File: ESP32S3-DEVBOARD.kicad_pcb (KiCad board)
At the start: 2 copper layers, 33 x 58.4 mm, 61 parts, among them J1 PinHeader_1x22_P2.54mm_Vertic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, J2 PinHeader_1x22_P2.54mm_Vertic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, J3 G-Switch_GT-USB-7010ASV, J4 G-Switch_GT-USB-7010ASV, Q1 BC817-40,215, Q2 BC817-40,215, SW1 TS-1088-AR02016, SW2 TS-1088-AR02016, SW3 TS-1088-AR02016, SW4 TS-1088-AR02016, U1 AMS1117-3.3, U2 ESP32-S3-WROOM-1, U3 USBLC6-2P6, U4 CP2102N-A02-GQFN28R, U5 BMI270, U6 USBLC6-2P6

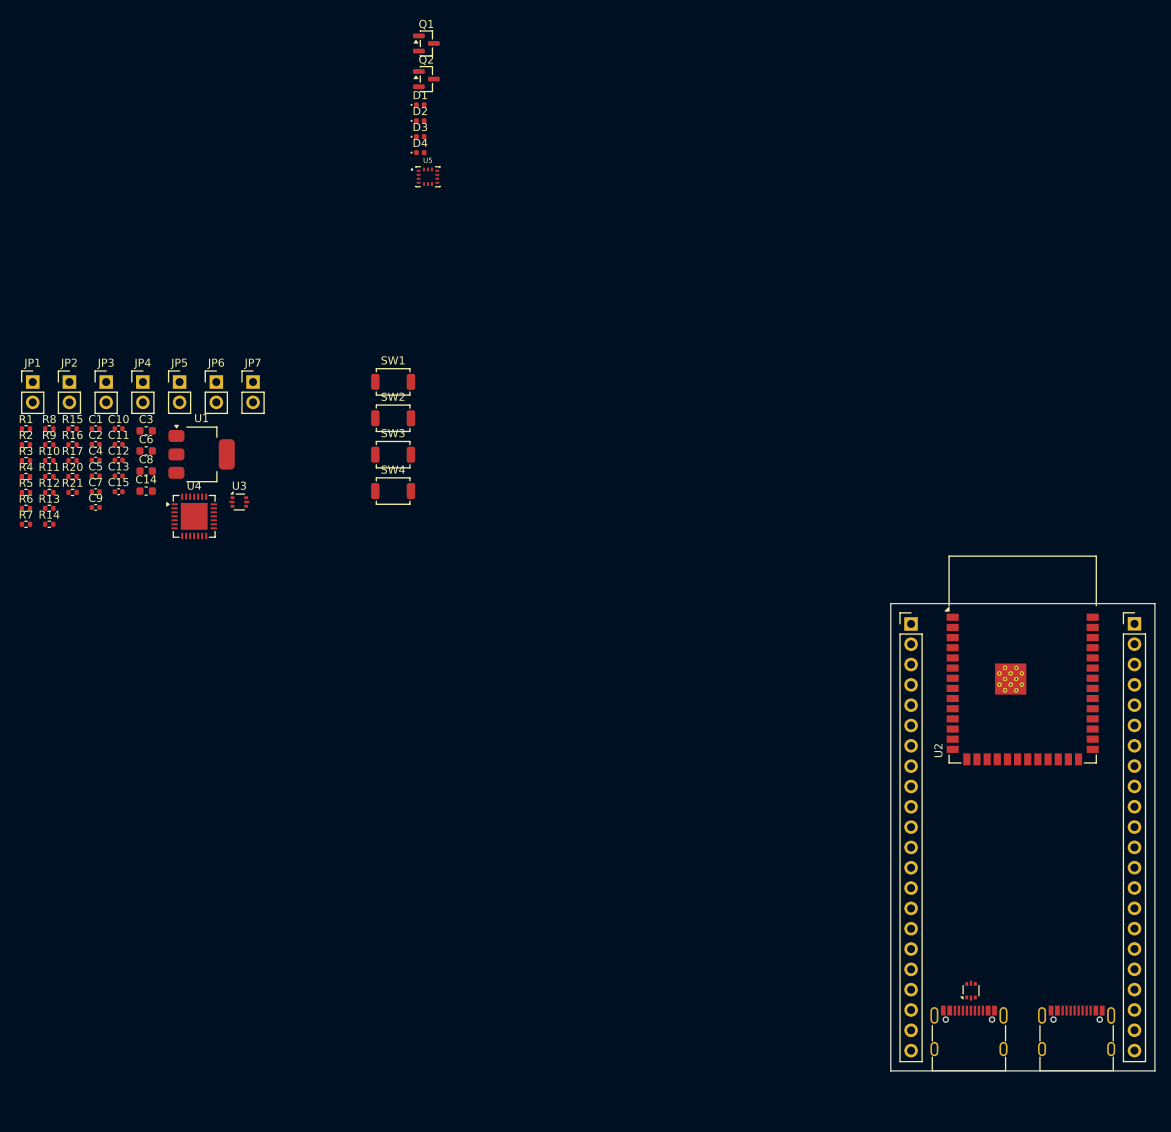
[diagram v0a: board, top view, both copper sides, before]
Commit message: Started to rout USB, need swap ports for uart
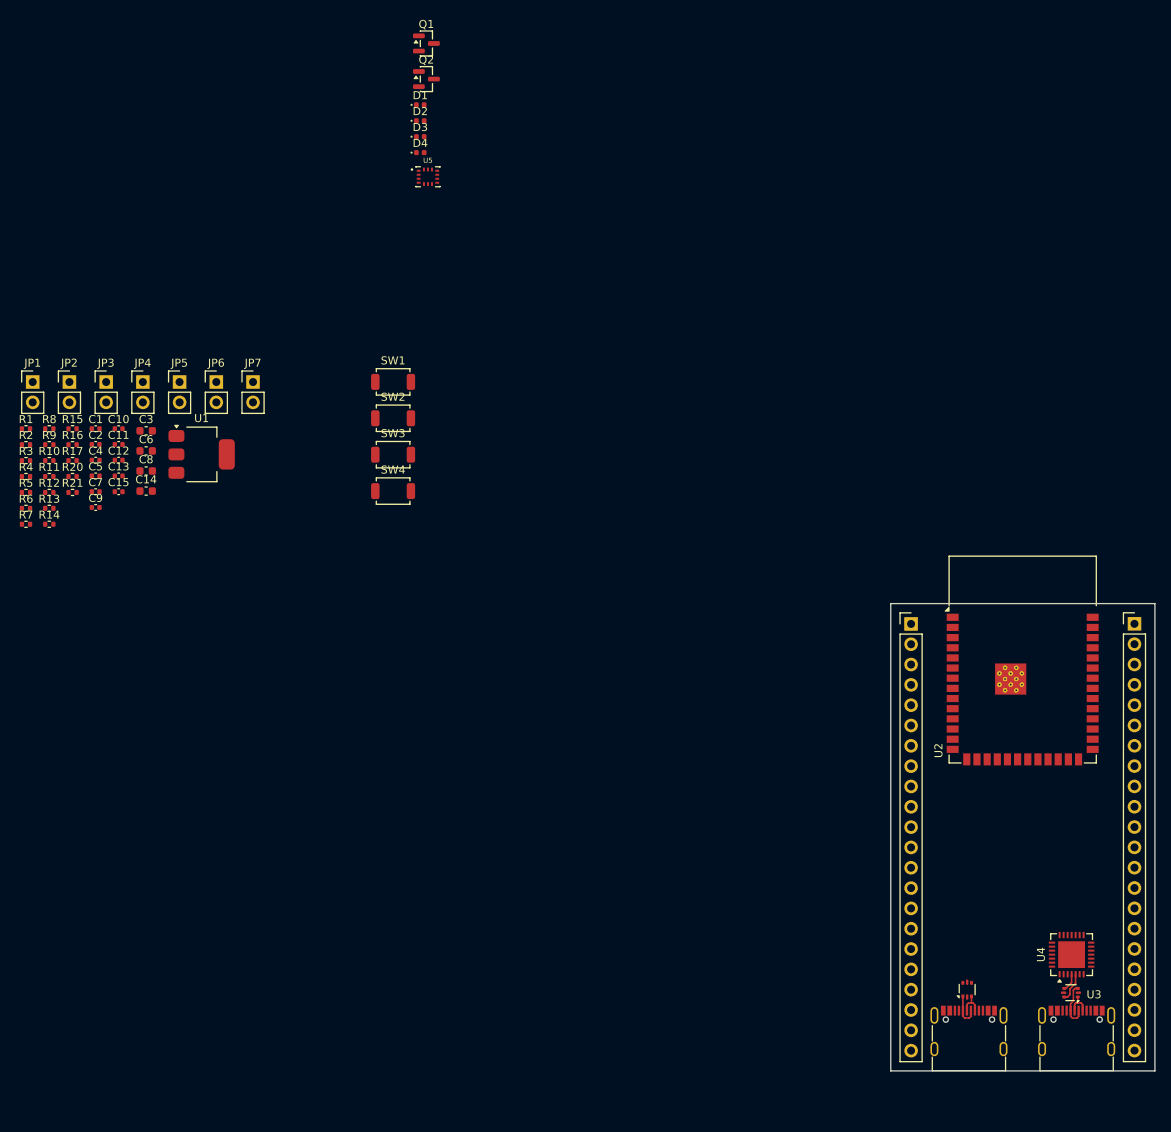
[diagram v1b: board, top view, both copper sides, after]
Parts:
- moved U4 122.6 mm to (162.3, 142.9), turned to 90 degrees
- moved U3 120.7 mm to (162.2, 147.7), turned to 180 degrees
- moved U6 0.50 mm to (149.3, 147.3)
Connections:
- U3 pad 1: Net-(J3-D--PadA7) -> Net-(J3-D+-PadA6)
- U3 pad 3: Net-(J3-D+-PadA6) -> Net-(J3-D--PadA7)
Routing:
- net Net-(J3-D--PadA7): track 0.00 -> 6.04 mm
- net Net-(J4-D--PadA7): track 0.00 -> 4.39 mm
- net /D_N: track 0.00 -> 3.68 mm
- net Net-(J4-D+-PadA6): track 0.00 -> 3.47 mm
- net Net-(J3-D+-PadA6): track 0.00 -> 3.45 mm
- net /D_P: track 0.00 -> 2.28 mm

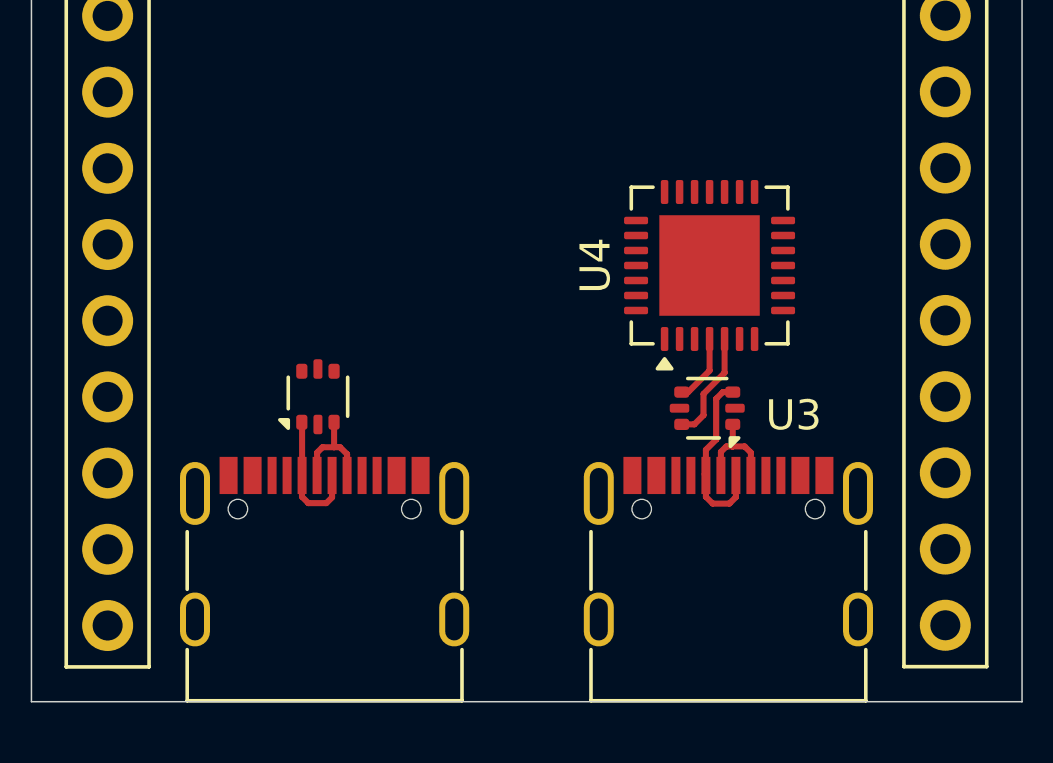
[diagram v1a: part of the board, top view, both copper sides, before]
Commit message: Swap usb ports, need to  define differential pair
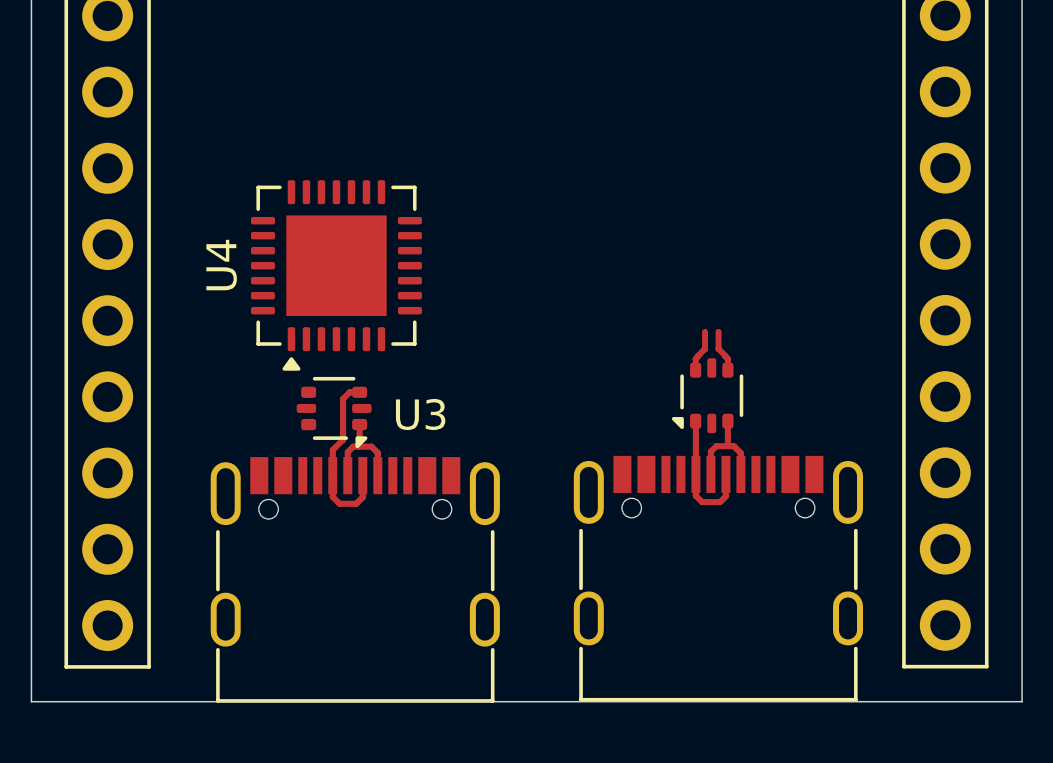
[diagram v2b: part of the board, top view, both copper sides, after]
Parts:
- moved J4 13.1 mm to (162.6, 153.6)
- moved U6 13.1 mm to (162.4, 147.3)
- moved U3 12.4 mm to (149.8, 147.7)
- moved U4 12.4 mm to (149.9, 143.0)
- moved J3 12.4 mm to (150.5, 153.7)
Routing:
- net /D_N: track 3.68 -> 0.00 mm
- net /D_P: track 2.28 -> 0.00 mm
- net /USB_D-: track 0.00 -> 1.41 mm
- net /USB_D+: track 0.00 -> 1.41 mm
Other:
- copper layers 2 -> 4

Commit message: Defined netclasses for USB
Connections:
- net Net-(J3-D+-PadA6) renamed /USB0_D+_T
- net Net-(J3-D--PadA7) renamed /USB0_D-_T
- net Net-(J4-D+-PadA6) renamed /USB1_D+_T
- net Net-(J4-D--PadA7) renamed /USB1_D-_T
- J2 pad 19: /USB_D+ -> /USB1_D+
- J2 pad 20: /USB_D- -> /USB1_D-
- U2 pad 13: /USB_D+ -> /USB1_D-
- U2 pad 14: /USB_D- -> /USB1_D+
- U3 pad 4: /D_P -> /USB0_D-
- U3 pad 6: /D_N -> /USB0_D+
- U4 pad 4: /D_P -> /USB0_D+
- U4 pad 5: /D_N -> /USB0_D-
- U6 pad 4: /USB_D+ -> /USB1_D+
- U6 pad 6: /USB_D- -> /USB1_D-
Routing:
- net /USB_D-: track 1.41 -> 0.00 mm
- net /USB_D+: track 1.41 -> 0.00 mm
- net /USB1_D-: track 0.00 -> 1.41 mm
- net /USB1_D+: track 0.00 -> 1.41 mm
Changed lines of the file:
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@@
 	(net 41 "/GPIO41")
 	(net 42 "/GPIO37")
-	(net 43 "/USB_D-")
+	(net 43 "/USB1_D-")
 	(net 44 "/GPIO36")
-	(net 45 "/USB_D+")
+	(net 45 "/USB1_D+")
 	(net 46 "/GPIO40")
 	(net 47 "/GPIO2")
 	(net 48 "/CC2")
 	(net 49 "unconnected-(J3-SBU1-PadA8)")
-	(net 50 "Net-(J3-D--PadA7)")
+	(net 50 "/USB0_D-_T")
 	(net 51 "unconnected-(J3-SBU2-PadB8)")
-	(net 52 "Net-(J3-D+-PadA6)")
+	(net 52 "/USB0_D+_T")
 	(net 53 "/CC1")
-	(net 54 "Net-(J4-D--PadA7)")
+	(net 54 "/USB1_D-_T")
 	(net 55 "unconnected-(J4-SBU2-PadB8)")
-	(net 56 "Net-(J4-D+-PadA6)")
+	(net 56 "/USB1_D+_T")
 	(net 57 "unconnected-(J4-SBU1-PadA8)")
 	(net 58 "/U2_TX")
@@
 	(net 70 "Net-(Q2-E)")
 	(net 71 "/U2_VBUS")
-	(net 72 "/D_N")
-	(net 73 "/D_P")
+	(net 72 "/USB0_D+")
+	(net 73 "/USB0_D-")
 	(net 74 "unconnected-(U4-~{RTS}-Pad24)")
 	(net 75 "unconnected-(U4-RS485{slash}GPIO.2-Pad17)")
@@
 			(layers "F.Cu" "F.Mask" "F.Paste")
 			(roundrect_rratio 0.25)
-			(net 54 "Net-(J4-D--PadA7)")
+			(net 54 "/USB1_D-_T")
 			(pinfunction "I/O1")
 			(pintype "passive")
@@
 			(layers "F.Cu" "F.Mask" "F.Paste")
 			(roundrect_rratio 0.25)
-			(net 56 "Net-(J4-D+-PadA6)")
+			(net 56 "/USB1_D+_T")
 			(pinfunction "I/O2")
 			(pintype "passive")
@@
 			(layers "F.Cu" "F.Mask" "F.Paste")
 			(roundrect_rratio 0.25)
-			(net 45 "/USB_D+")
+			(net 45 "/USB1_D+")
 			(pinfunction "I/O2")
 			(pintype "passive")
@@
 			(layers "F.Cu" "F.Mask" "F.Paste")
 			(roundrect_rratio 0.25)
-			(net 43 "/USB_D-")
+			(net 43 "/USB1_D-")
 			(pinfunction "I/O1")
 			(pintype "passive")
@@
 			(size 0.3 1.24)
 			(layers "F.Cu" "F.Mask" "F.Paste")
-			(net 52 "Net-(J3-D+-PadA6)")
+			(net 52 "/USB0_D+_T")
 			(pinfunction "D+")
 			(pintype "bidirectional")
@@
 			(size 0.3 1.24)
 			(layers "F.Cu" "F.Mask" "F.Paste")
-			(net 50 "Net-(J3-D--PadA7)")
+			(net 50 "/USB0_D-_T")
 			(pinfunction "D-")
 			(pintype "bidirectional")
@@
 			(size 0.3 1.24)
 			(layers "F.Cu" "F.Mask" "F.Paste")
-			(net 52 "Net-(J3-D+-PadA6)")
+			(net 52 "/USB0_D+_T")
 			(pinfunction "D+")
 			(pintype "bidirectional")
@@
 			(size 0.3 1.24)
 			(layers "F.Cu" "F.Mask" "F.Paste")
-			(net 50 "Net-(J3-D--PadA7)")
+			(net 50 "/USB0_D-_T")
 			(pinfunction "D-")
 			(pintype "bidirectional")
@@
 			(size 1.5 0.9)
 			(layers "F.Cu" "F.Mask" "F.Paste")
-			(net 45 "/USB_D+")
+			(net 43 "/USB1_D-")
 			(pinfunction "USB_D-")
 			(pintype "bidirectional")
@@
 			(size 1.5 0.9)
 			(layers "F.Cu" "F.Mask" "F.Paste")
-			(net 43 "/USB_D-")
+			(net 45 "/USB1_D+")
 			(pinfunction "USB_D+")
 			(pintype "bidirectional")
@@
 			(layers "*.Cu" "*.Mask")
 			(remove_unused_layers no)
-			(net 45 "/USB_D+")
+			(net 45 "/USB1_D+")
 			(pinfunction "Pin_19")
 			(pintype "passive")
@@
 			(layers "*.Cu" "*.Mask")
 			(remove_unused_layers no)
-			(net 43 "/USB_D-")
+			(net 43 "/USB1_D-")
 			(pinfunction "Pin_20")
 			(pintype "passive")
@@
 			(layers "F.Cu" "F.Mask" "F.Paste")
 			(roundrect_rratio 0.25)
-			(net 73 "/D_P")
+			(net 72 "/USB0_D+")
 			(pinfunction "D+")
 			(pintype "bidirectional")
@@
 			(layers "F.Cu" "F.Mask" "F.Paste")
 			(roundrect_rratio 0.25)
-			(net 72 "/D_N")
+			(net 73 "/USB0_D-")
 			(pinfunction "D-")
 			(pintype "bidirectional")
@@
 			(layers "F.Cu" "F.Mask" "F.Paste")
 			(roundrect_rratio 0.25)
-			(net 52 "Net-(J3-D+-PadA6)")
+			(net 52 "/USB0_D+_T")
 			(pinfunction "I/O1")
 			(pintype "passive")
@@
 			(layers "F.Cu" "F.Mask" "F.Paste")
 			(roundrect_rratio 0.25)
-			(net 50 "Net-(J3-D--PadA7)")
+			(net 50 "/USB0_D-_T")
 			(pinfunction "I/O2")
 			(pintype "passive")
@@
 			(layers "F.Cu" "F.Mask" "F.Paste")
 			(roundrect_rratio 0.25)
-			(net 73 "/D_P")
+			(net 73 "/USB0_D-")
 			(pinfunction "I/O2")
 			(pintype "passive")
@@
 			(layers "F.Cu" "F.Mask" "F.Paste")
 			(roundrect_rratio 0.25)
-			(net 72 "/D_N")
+			(net 72 "/USB0_D+")
 			(pinfunction "I/O1")
 			(pintype "passive")
@@
 			(size 0.3 1.24)
 			(layers "F.Cu" "F.Mask" "F.Paste")
-			(net 56 "Net-(J4-D+-PadA6)")
+			(net 56 "/USB1_D+_T")
 			(pinfunction "D+")
 			(pintype "bidirectional")
@@
 			(size 0.3 1.24)
 			(layers "F.Cu" "F.Mask" "F.Paste")
-			(net 54 "Net-(J4-D--PadA7)")
+			(net 54 "/USB1_D-_T")
 			(pinfunction "D-")
 			(pintype "bidirectional")
@@
 			(size 0.3 1.24)
 			(layers "F.Cu" "F.Mask" "F.Paste")
-			(net 56 "Net-(J4-D+-PadA6)")
+			(net 56 "/USB1_D+_T")
 			(pinfunction "D+")
 			(pintype "bidirectional")
@@
 			(size 0.3 1.24)
 			(layers "F.Cu" "F.Mask" "F.Paste")
-			(net 54 "Net-(J4-D--PadA7)")
+			(net 54 "/USB1_D-_T")
 			(pinfunction "D-")
 			(pintype "bidirectional")

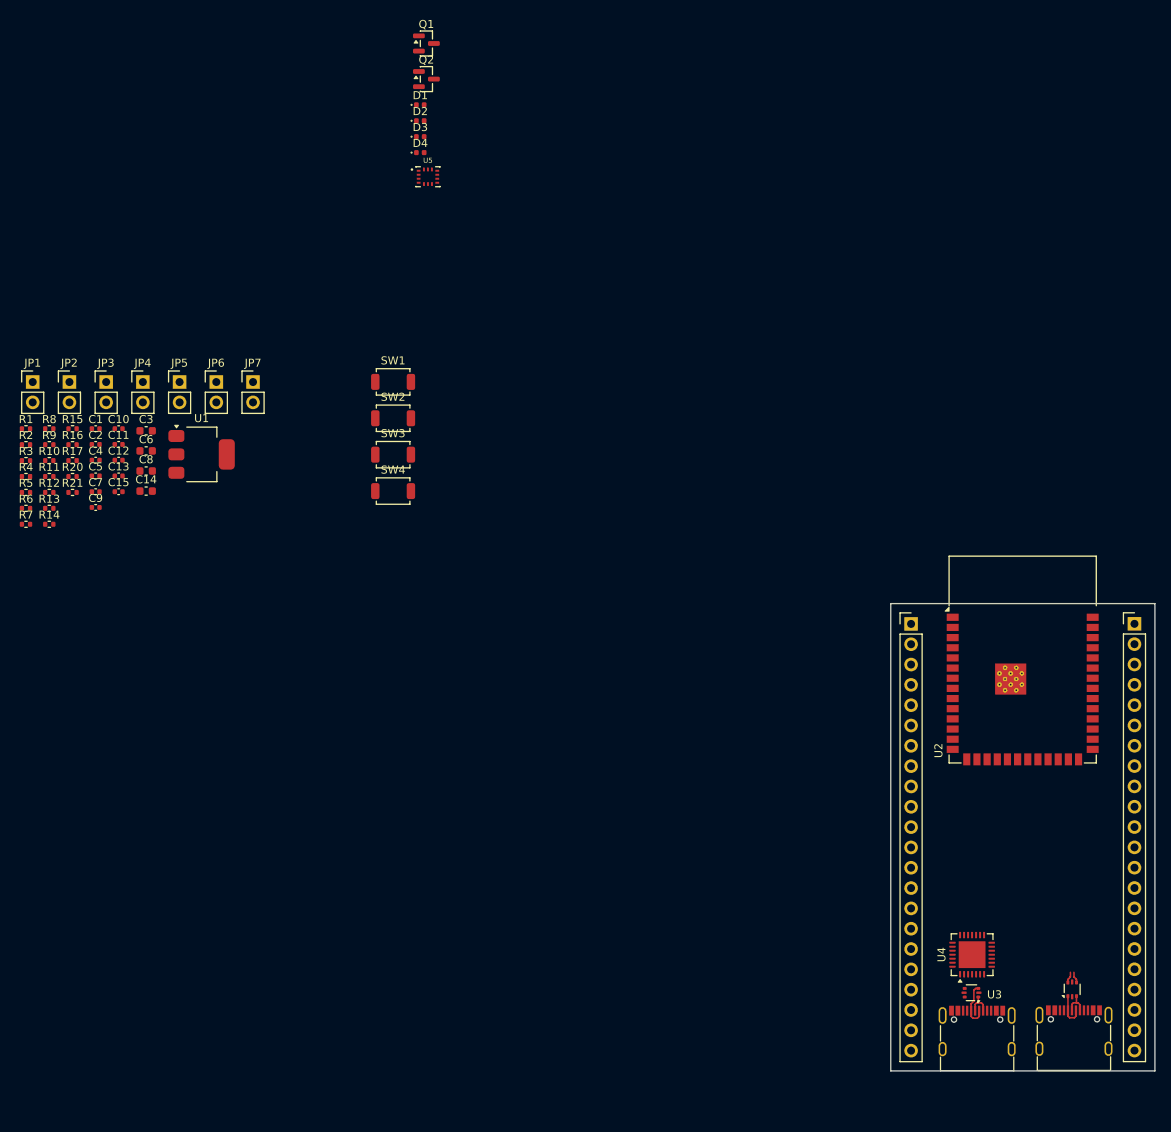
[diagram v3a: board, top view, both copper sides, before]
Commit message: Routed USB and added uart jumpers
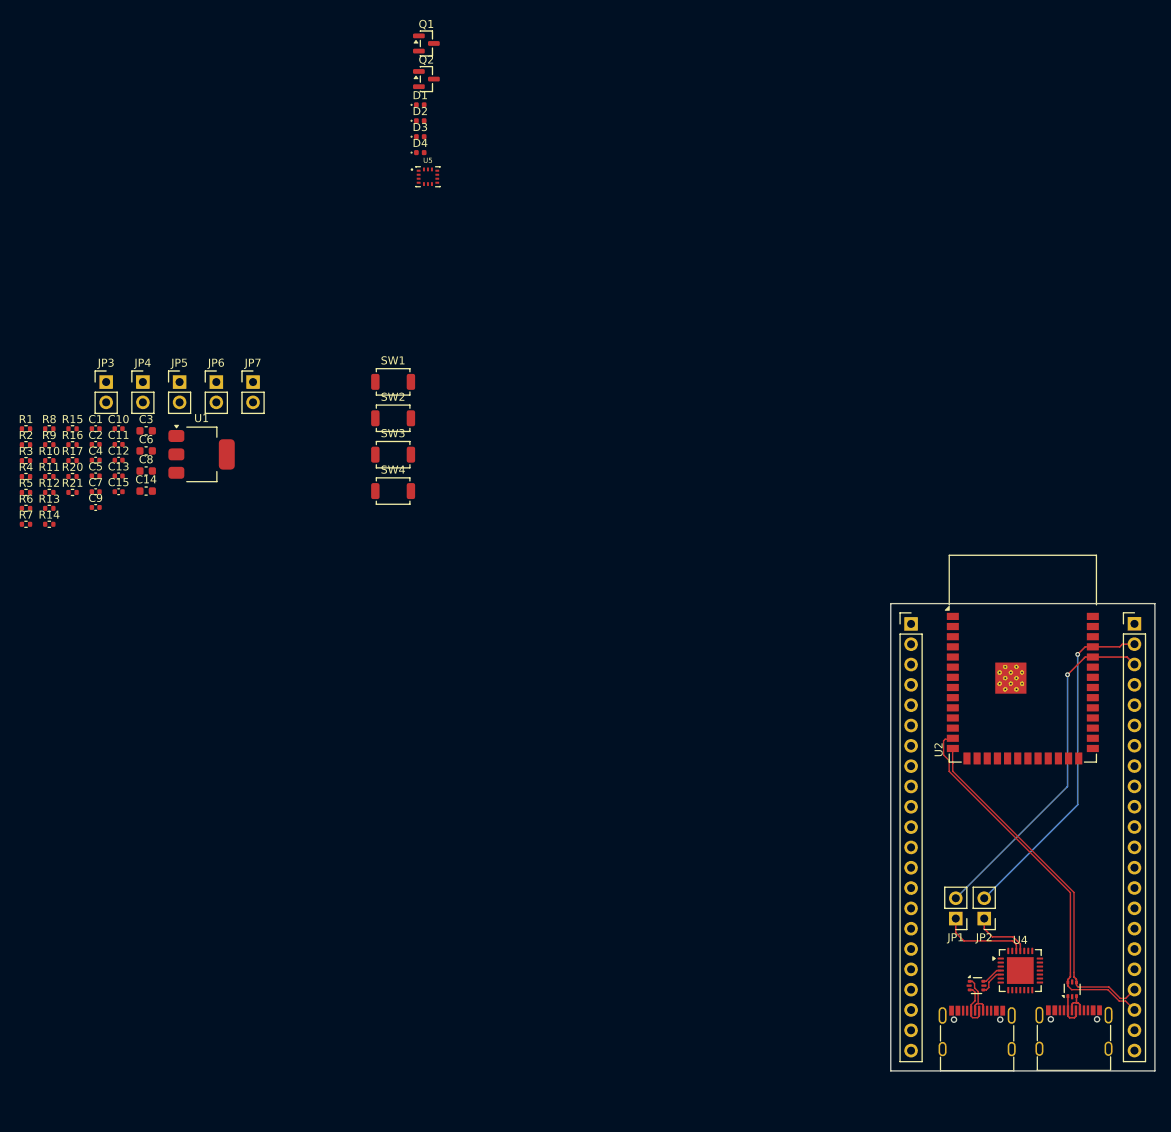
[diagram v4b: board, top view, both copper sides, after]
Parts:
- moved JP1 133.5 mm to (147.8, 138.4), turned to 180 degrees
- moved JP2 132.6 mm to (151.4, 138.4), turned to 180 degrees
- moved U4 6.34 mm to (155.9, 144.9), turned to 0 degrees
- moved U3 1.09 mm to (150.4, 146.8), turned to 0 degrees
- moved U2 0.11 mm to (156.2, 105.9)
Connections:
- net /USB0_D+_T renamed /USB0_T_D+
- net /USB0_D-_T renamed /USB0_T_D-
- net /USB1_D+_T renamed /USB1_T_D+
- net /USB1_D-_T renamed /USB1_T_D-
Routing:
- net /USB1_D-: track 1.41 -> 48.1 mm
- net /GPIO44: track 0.00 -> 43.4 mm, vias 0 -> 1
- net /GPIO43: track 0.00 -> 42.9 mm, vias 0 -> 1
- net /USB1_D+: track 1.41 -> 44.3 mm
- net /U2_TX: track 0.00 -> 10.8 mm
- net /U2_RX: track 0.00 -> 7.44 mm
- net /USB0_D-: track 0.00 -> 3.35 mm
- net /USB0_D+: track 0.00 -> 2.73 mm
- net /USB0_T_D+: track 3.45 -> 5.96 mm
